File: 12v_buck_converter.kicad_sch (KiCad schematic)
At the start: 25 parts, among them IC1 TPS56A37RPAR, Q4 SI7149ADP-T1-GE3, Q5 SI7149ADP-T1-GE3, U3 MAX16914AUB+

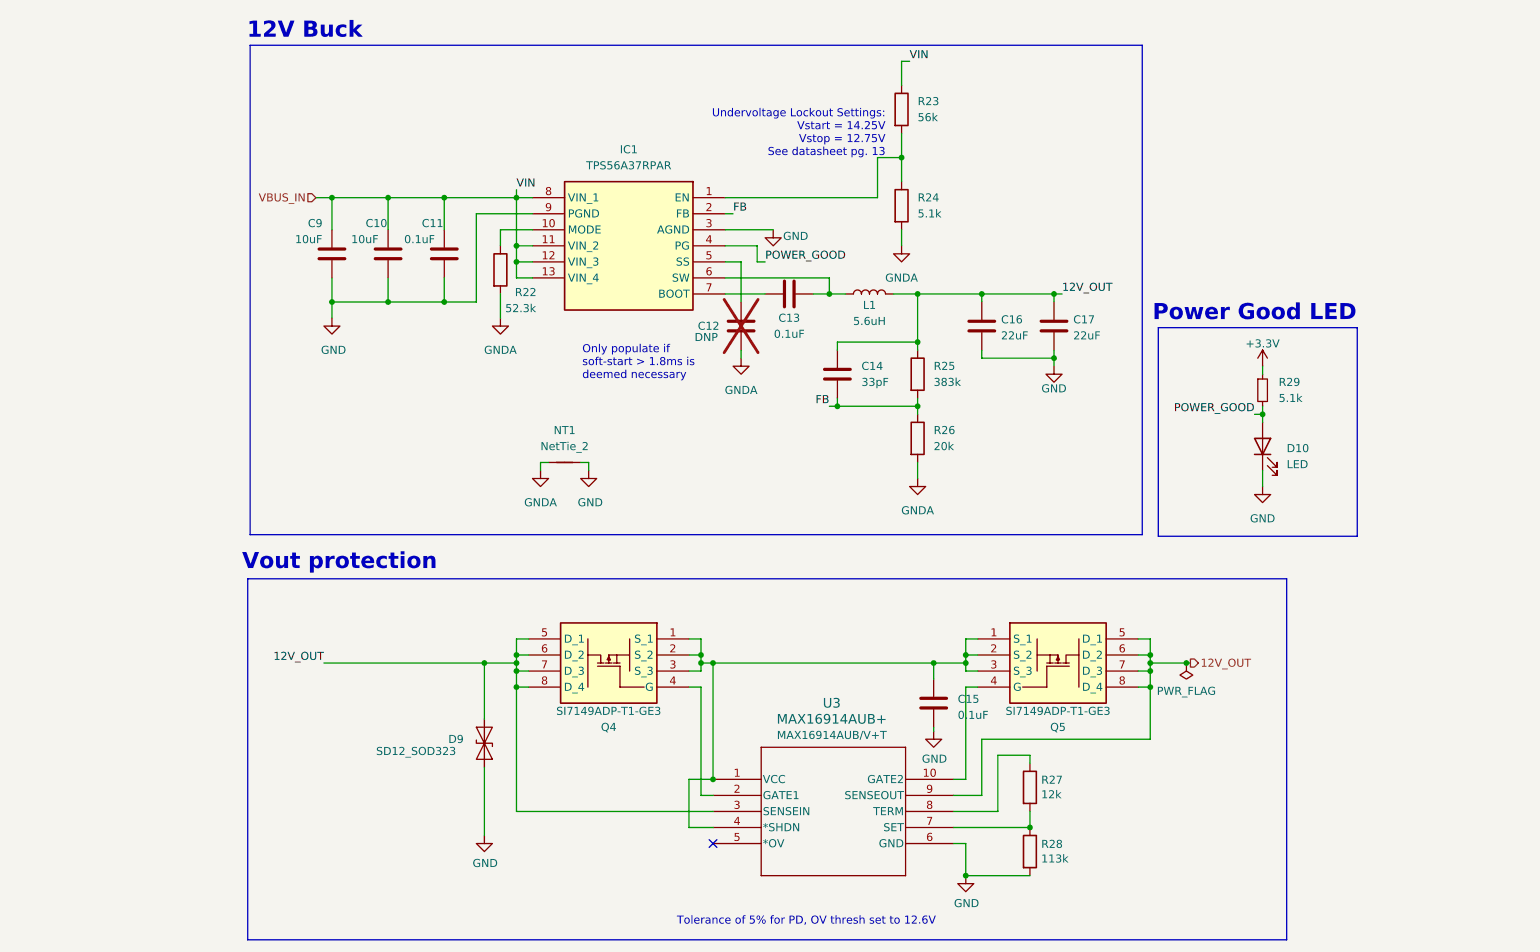
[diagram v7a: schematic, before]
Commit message: Addressed most of the review comments, fixed power protection, added bigger caps & better part selection on 12V and 5V out, changed 5V buck inductor, fixed power good & fault LEDs
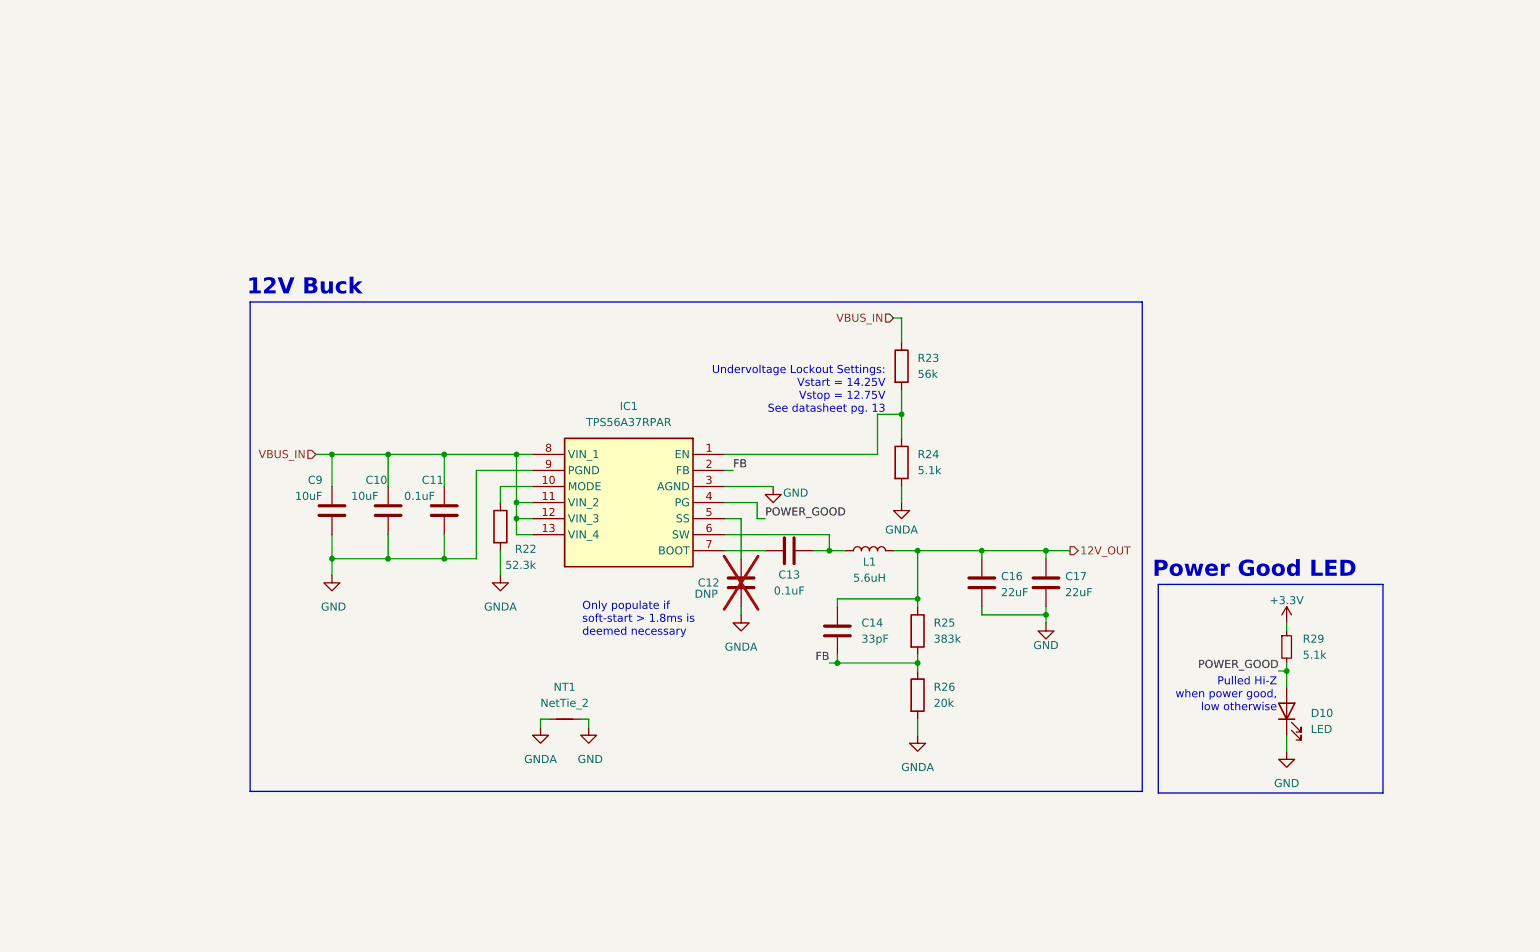
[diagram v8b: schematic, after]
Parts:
- removed C15: 0.1uF, Capacitor_SMD:C_0805_2012Metric, symbol Device:C
- removed D9: SD12_SOD323, Diode_SMD:D_SOD-323, symbol Diode:SD12_SOD323
- removed Q4, Q5: SI7149ADP-T1-GE3, UTSVT_ICs:POWERPAKSO-8, symbol utsvt-chips:SI7149ADP-T1-GE3
- removed R27: 12k, Resistor_SMD:R_0805_2012Metric, symbol Device:R
- removed R28: 113k, Resistor_SMD:R_0805_2012Metric, symbol Device:R
- removed U3: MAX16914AUB+, UTSVT_ICs:21-0061L_MXM, symbol utsvt-chips:MAX16914AUB_V+T
- C16, C17: footprint Capacitor_SMD:C_0805_2012Metric -> Capacitor_SMD:C_1210_3225Metric; Manufacturer_Name TDK -> Taiyo Yuden; Mouser Part Number C2012X5R1V226M125AC -> GMK325BJ226MM-P
- L1: Mouser Part Number 652-SRP1038CC-5R6M -> SRP1038CC-5R6M
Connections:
- no-connect marks 1 -> 0
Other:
- note added: "Pulled Hi-Z when power good, low otherwise"
- note removed: "Tolerance of 5% for PD, OV thresh set to 12.6V"
- note removed: "Vout protection"
- moved on the sheet: C10, C11, C12, C13, C14, C16, C17, C9, D10, IC1, L1, NT1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
